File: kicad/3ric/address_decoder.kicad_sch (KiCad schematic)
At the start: 39 parts

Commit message: updates to logisim project and schematics
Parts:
- U? (x12): value (none) -> 74LS00
- U? (x21): value (none) -> 74LS32
- U? (x2): value (none) -> 74LS08
- U? (x2): value (none) -> 74LS14
- U?: value (none) -> 74LS154
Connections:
- net X0: now also U?.1
- net X30: no longer U?.1

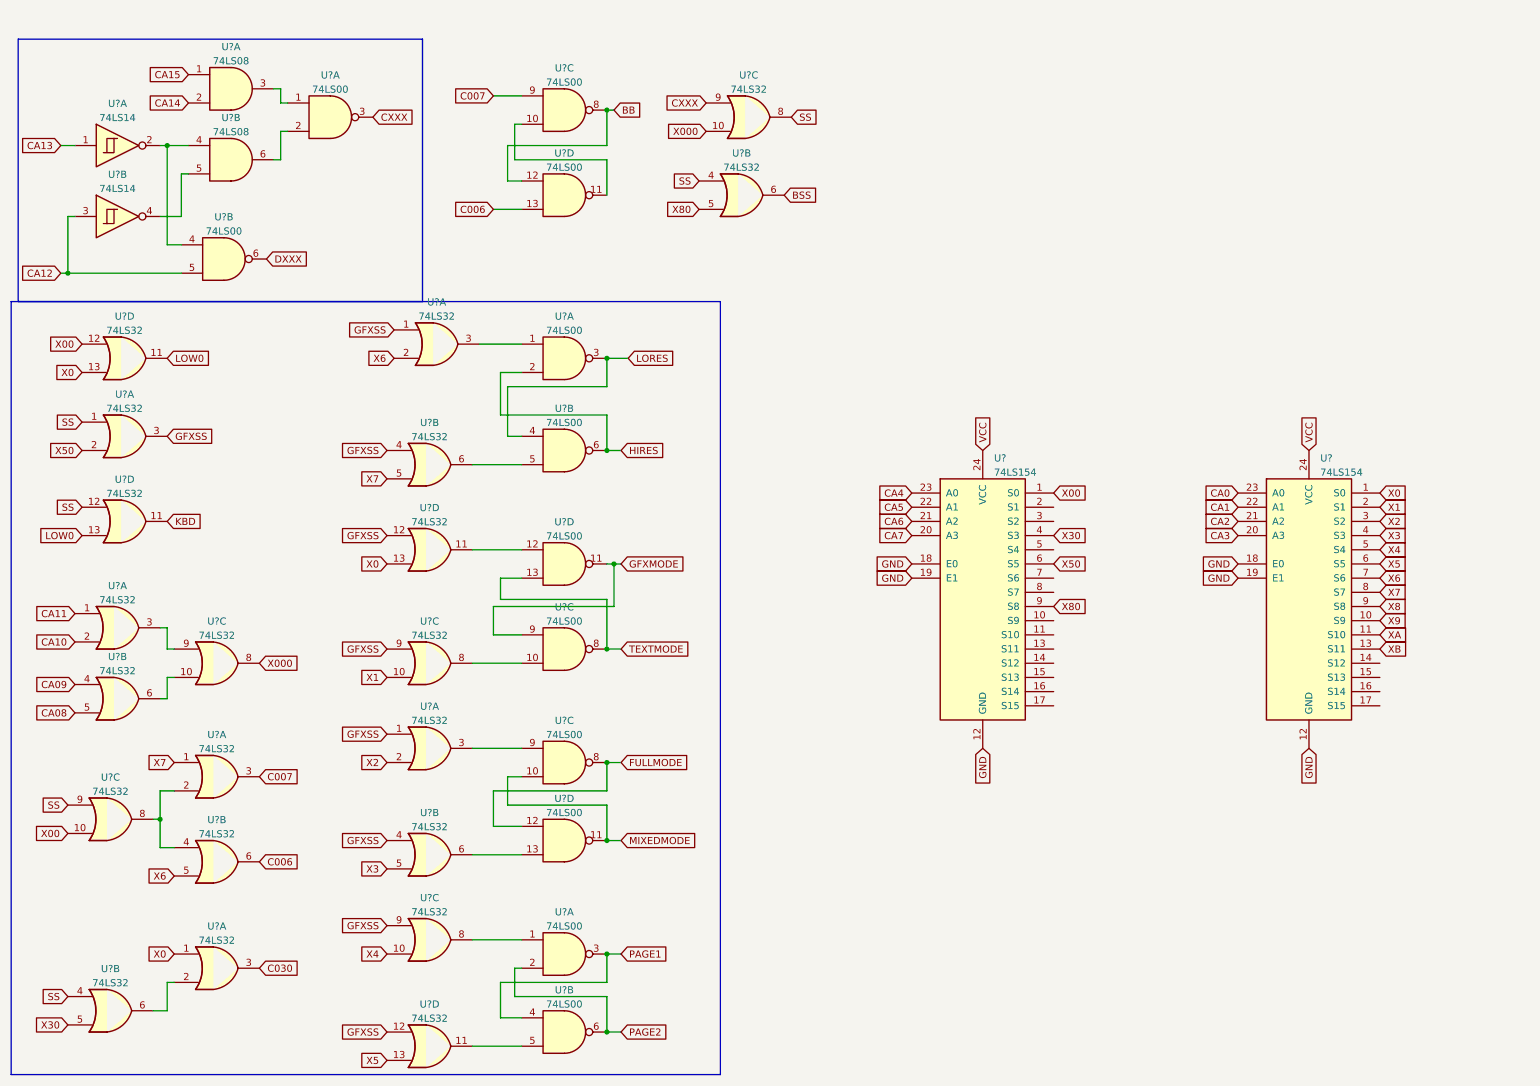
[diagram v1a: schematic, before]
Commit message: move some of the logic to PLD, move device range from C1XX to CX00 update device labels to be more correct update PLD
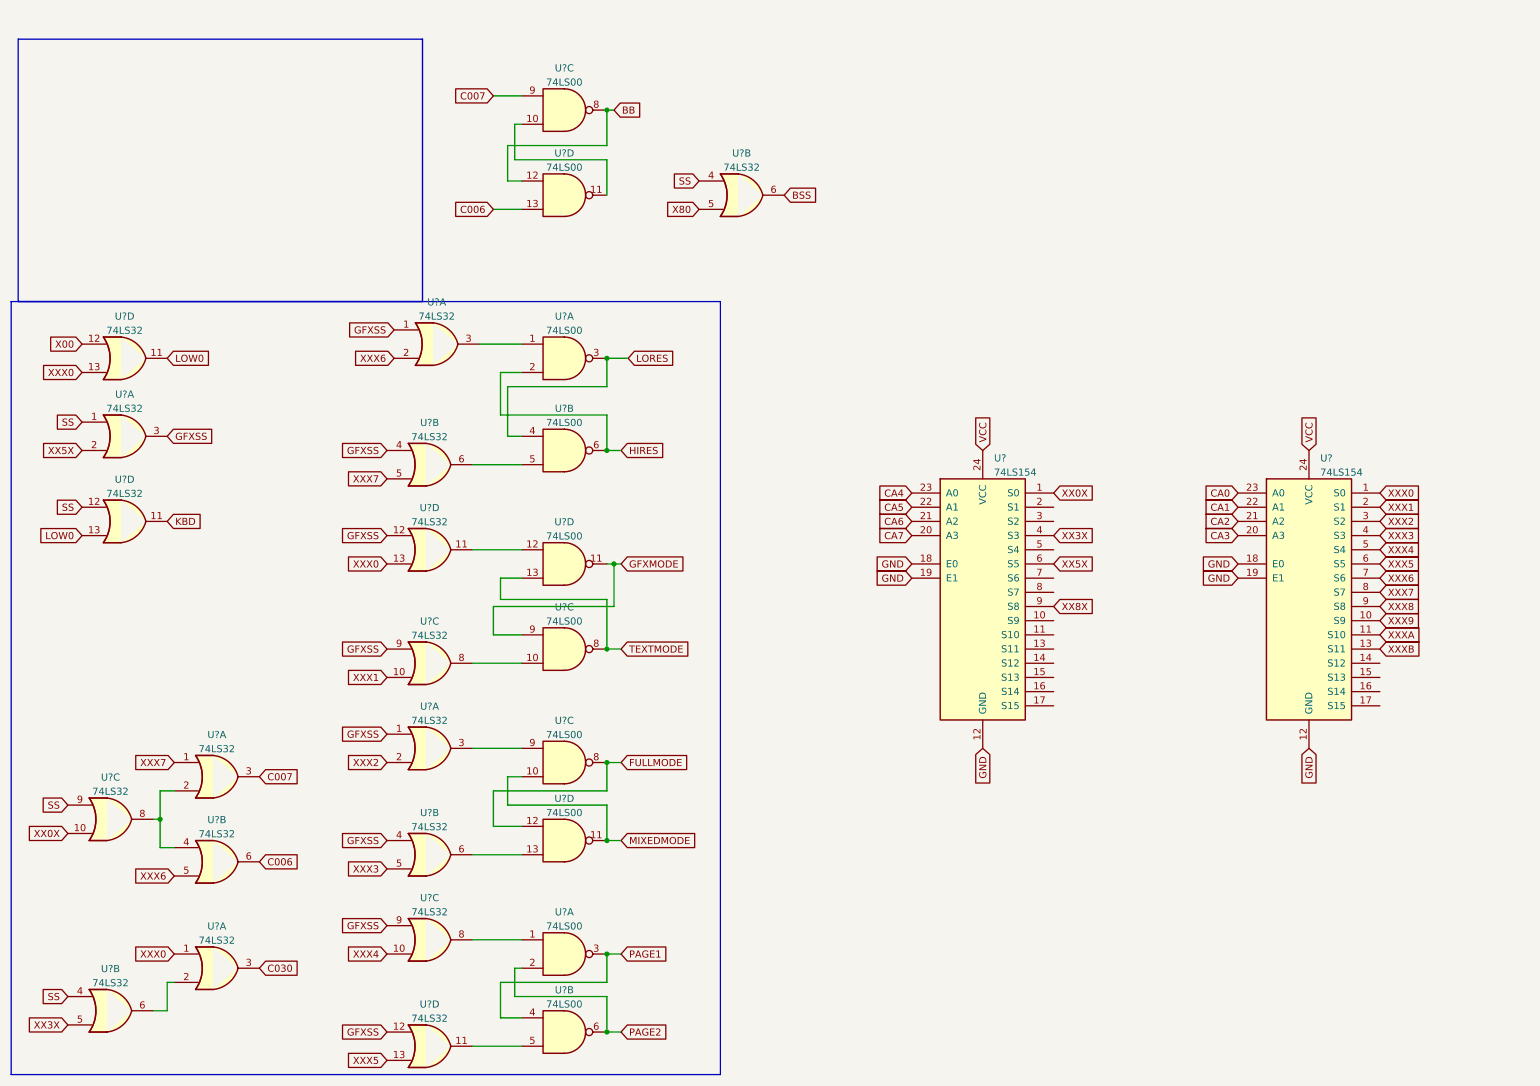
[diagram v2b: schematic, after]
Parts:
- removed U? (x2): 74LS08, symbol 74xx:74LS08
- removed U? (x4): 74LS32, symbol 74xx:74LS32
- removed U? (x2): 74LS00, symbol 74xx:74LS00
- removed U? (x2): 74LS14, symbol 74xx:74LS14
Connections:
- net X00: no longer U?.1 (S0), U?.10
- net X80: no longer U?.9 (S8)
- net X0 renamed XXX0
- net X1 renamed XXX1
- net X2 renamed XXX2
- net X3 renamed XXX3
- net X30 renamed XX3X
- net X4 renamed XXX4
- net X5 renamed XXX5
- net X50 renamed XX5X
- net X6 renamed XXX6
- net X7 renamed XXX7
- net X8 renamed XXX8
- net X9 renamed XXX9
- net XA renamed XXXA
- net XB renamed XXXB
- new net XX0X: U?.1 (S0), U?.10
- new net XX8X: U?.9 (S8)

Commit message: push schematic updates
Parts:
- removed U? (x10): 74LS00, symbol 74xx:74LS00
- removed U? (x17): 74LS32, symbol 74xx:74LS32
- removed U? (x2): 74LS154, symbol 74xx:74LS154
- added U? (x7): 74LS04, symbol 74xx:74LS04
- added U? (x14): 74LS32, symbol 74xx:74LS32
- added U? (x14): 74LS08, symbol 74xx:74LS08
- added U? (x5): 74LS00, symbol 74xx:74LS00
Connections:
- net BB: now also U?.10
- net KBD: now also U?.5
- new net: U?.12, U?.6 (x2)
- new net: U?.13, U?.3
- new net: U?.4, U?.8
- new net: U?.3, U?.9
- new net: U?.2, U?.6
- new net: U?.1, U?.1, U?.3
- new net: U?.13, U?.8
- new net: U?.2, U?.8
- new net: U?.11, U?.12
- new net: U?.5, U?.8
- new net: U?.5, U?.6
- new net: U?.8, U?.9
- new net: U?.10, U?.8
- new net: U?.12, U?.8
- new net: U?.10, U?.11
- new net: U?.4, U?.5, U?.8
- new net: U?.13, U?.6
- new net: U?.1, U?.3
- new net: U?.3, U?.5
- new net: U?.4, U?.6
- new net: U?.10, U?.6
- new net: U?.2, U?.3, U?.9
- new net !CA12: U?.1, U?.2, U?.5
- new net !CA13: U?.2, U?.4, U?.4, U?.9
- new net !R~{W}: U?.12, U?.13, U?.2
- new net !VIDENABLE: U?.1, U?.12, U?.12, U?.9
- new net A13|A12: U?.1, U?.3, U?.5
- new net A16: U?.11
- new net B2: U?.4
- new net CA10: U?.5
- new net CA11: U?.4, U?.4
- new net CA12: U?.1, U?.1, U?.10
- new net CA13: U?.2, U?.3
- new net CA14: U?.1, U?.2, U?.9
- new net CA15: U?.1, U?.2, U?.2
- new net CA8: U?.2
- new net CA9: U?.1
- new net CXXX: U?.3
- new net DXXX: U?.3, U?.9
- new net PHI2: U?.13, U?.9
- new net RAMREAD: U?.9
- new net RAMWRITE: U?.12
- new net R~{W}: U?.10, U?.13, U?.9
- new net VIDBUS: U?.2
- new net X0XX: U?.11
- new net ~{CS_CPUBUS}: U?.8
- new net ~{CS_DEVICE}: U?.11
- new net ~{CS_RAM}: U?.3
- new net ~{CS_ROM}: U?.11
- new net ~{DEVICE}: U?.10, U?.11, U?.13
- new net ~{OE}: U?.3
- new net ~{RAM}: U?.1, U?.10, U?.8
- new net ~{ROM}: U?.13, U?.6, U?.9
- new net ~{WE}: U?.8

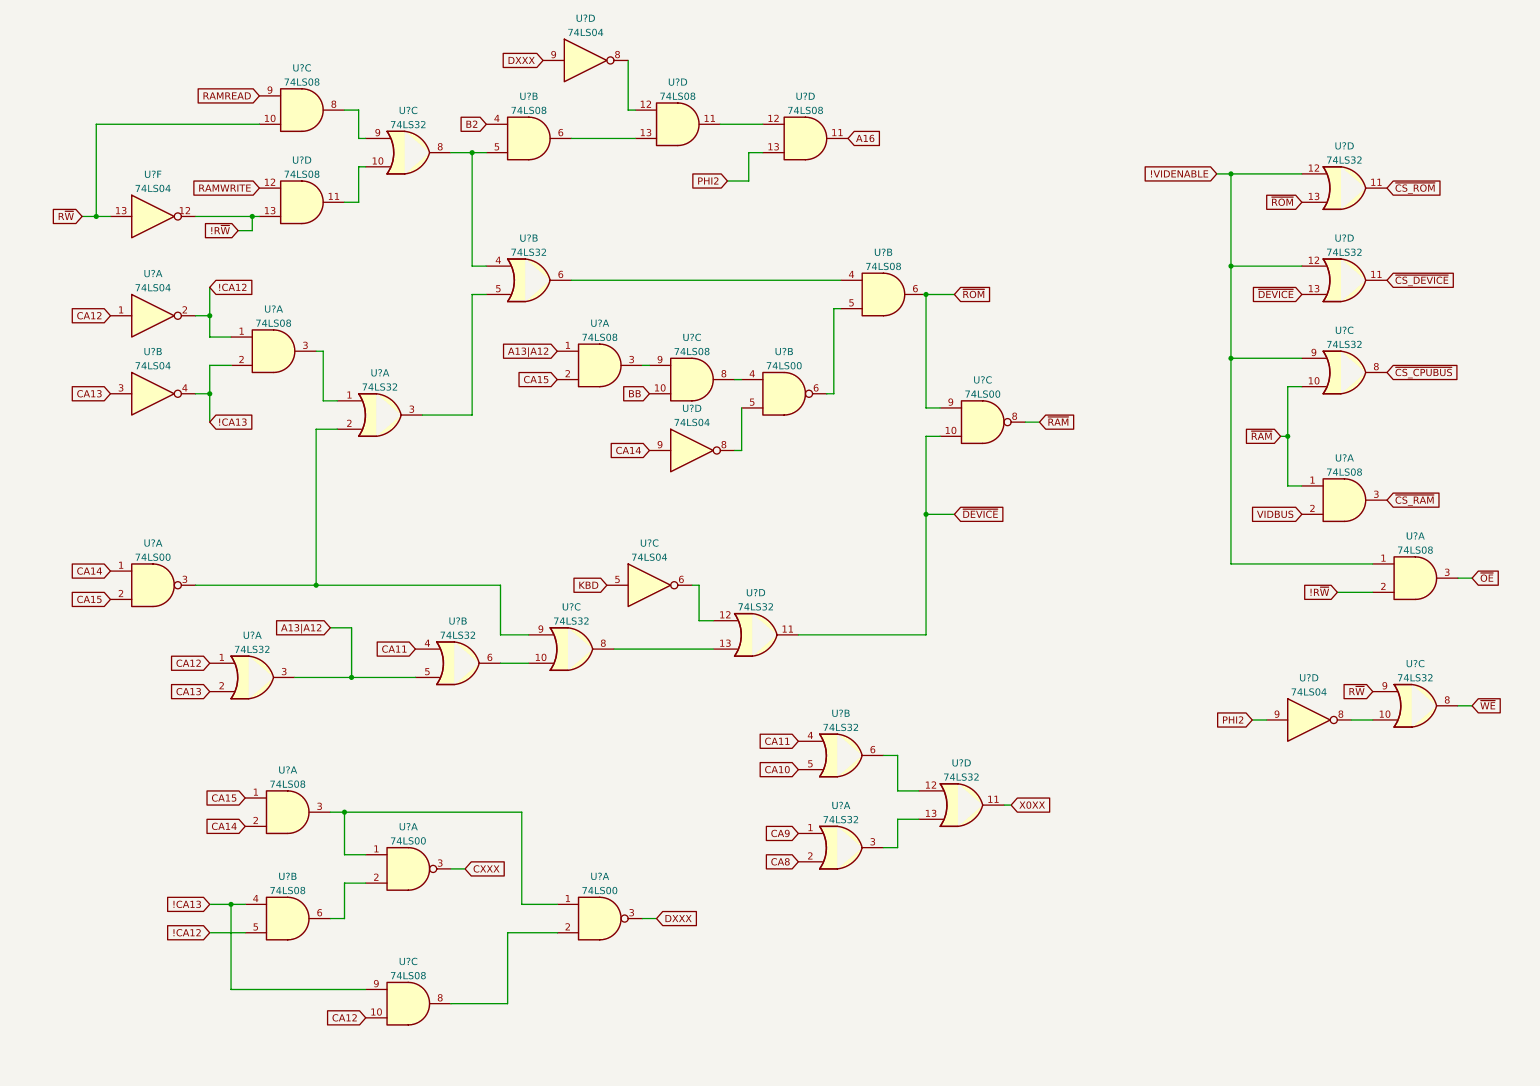
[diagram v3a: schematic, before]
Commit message: upgraded to kicad 8, updates to schematic - added snes controllers, mouse port, many fixes
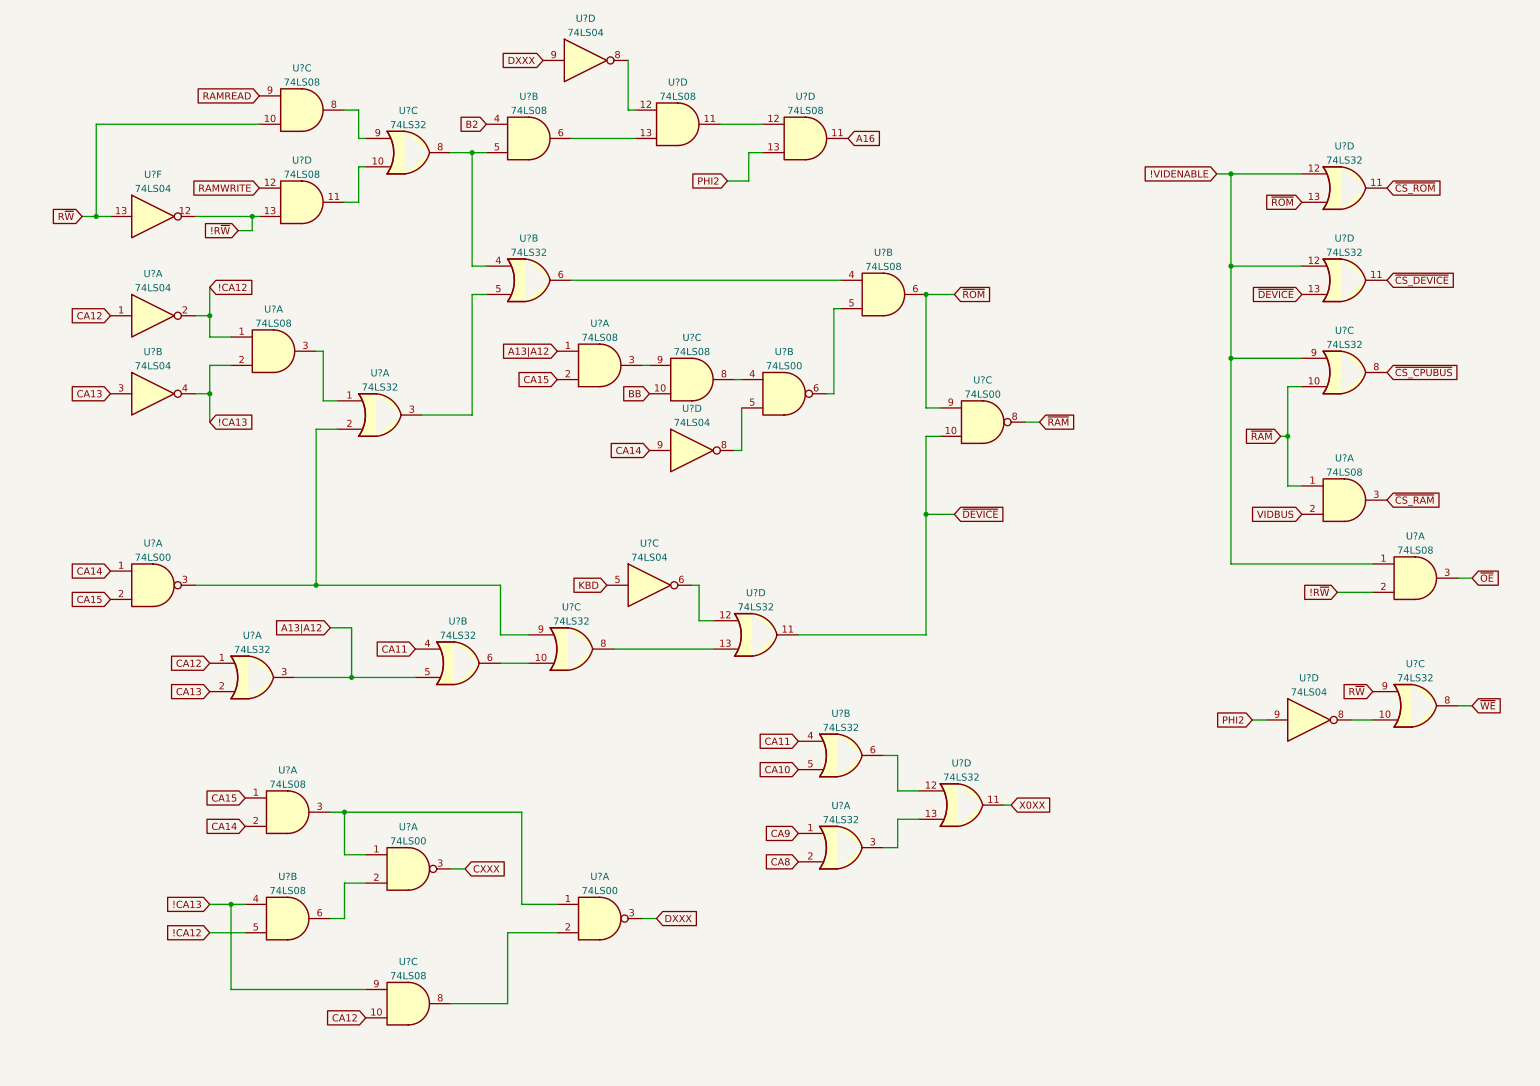
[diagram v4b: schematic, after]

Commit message: schematic updates
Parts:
- added U1: 74LS00, symbol 74xx:74LS00
- added U2, U5: 74LS32, symbol 74xx:74LS32
- added U3: 74LS04, symbol 74xx:74LS04
- added U4: 74LS08, symbol 74xx:74LS08
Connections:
- net CA10: now also U1.1
- net CA11: now also U5.4
- net CA9: now also U1.2
- net CXXX: now also U2.2
- net at U?.13: now also U2.8; no longer U?.8
- net at U?.6: now also U4.5; no longer U?.4
- new net: U1.3, U2.1
- new net: U2.9, U?.8
- new net: U4.4, U5.6
- new net: U4.6, U?.4
- new net !C6XX: U2.10, U3.6
- new net C6XX: U2.3, U3.5, U5.5
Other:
- moved on the sheet: U?B, U?D
